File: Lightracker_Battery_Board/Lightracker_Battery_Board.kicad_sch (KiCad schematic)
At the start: 5 parts, among them J1 B2B-XH-A, J2 Conn_02x08_Odd_Even, J3 Conn_02x08_Odd_Even, U1 DF Robot DC-DC Converter, U2 Light Tracker Lora APRS Unit

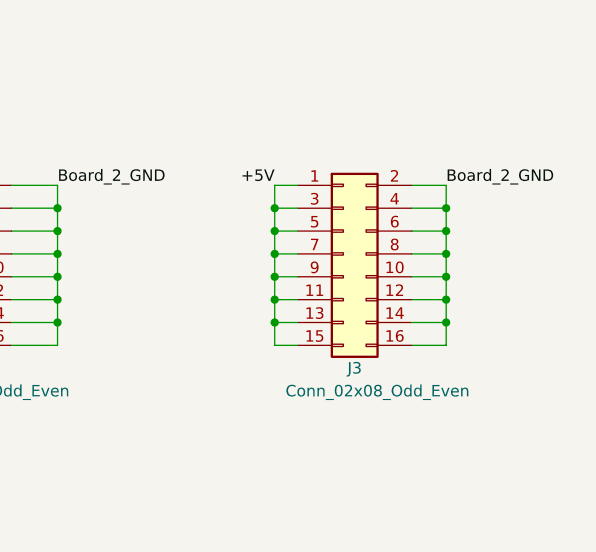
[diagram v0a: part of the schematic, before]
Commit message: Fix flipped components
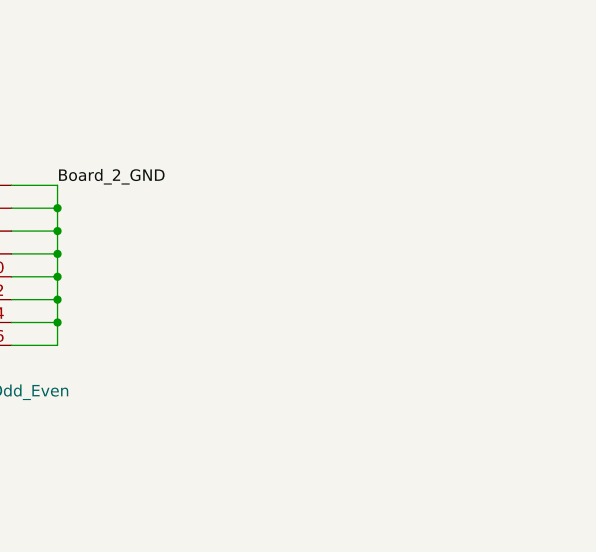
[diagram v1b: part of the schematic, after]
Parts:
- removed J3: Conn_02x08_Odd_Even, Connector_PinHeader_2.54mm:PinHeader_2x08_P2.54mm_Vertical, symbol Connector_Generic:Conn_02x08_Odd_Even
